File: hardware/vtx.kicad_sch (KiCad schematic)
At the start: 58 parts, among them J1 U.FL, Q27 BC857BM, Q28 AP1606, U19 RTC6705, U20 SE5004L, U21 LP5912-3.3, U22 LP5907-2.85, X4 8MHz 10pF

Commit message: wip: schematic integration in progress (saved after container restart)
Co-Authored-By: Claude Opus 5.5 <noreply@anthropic.com>
Claude-Session: https://claude.ai/code/session_01RFaS5jnC9tnPam9GBgmGnG
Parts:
- C108, C118: LCSC (none) -> C237279
- Q28: symbol OpenDrone:AP1606 -> lib:AP1606
- R84: value 10k -> 1k; LCSC C106225 -> (none); MPN RC0201FR-0710KL -> RC0201FR-071KL
- U21: symbol OpenDrone:LP5912-3.3DRVR -> lib:LP5912-3.3DRVR
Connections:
- net PA_RC1: now reaches C124.1, R71.2, R72.1
- net Q27_B: now reaches C125.1, Q27.1 (B), R72.2
- net U19_SPILE: now reaches R80.2, U19.6 (SPILE/CS1)
- net VT_MOD: now reaches R60.2, R61.2, R62.1, U19.10 (VT_Mod)
- net VT_MOD_N1: now reaches C104.2, C105.1, R58.2, R59.1
- net U19_XTAL2: now reaches C95.1, U19.25 (XTAL2), X4.3
- net Q27_E: now reaches Q27.2 (E), R73.2
- net VT_MOD_N2: now reaches C105.2, R60.1
- net U19_REG1D8: now reaches C96.1, U19.23 (REG1D8_1)
- net RTC_LF: now reaches C107.1, R64.2
- net U19_XTAL1: now reaches C94.1, U19.24 (XTAL1), X4.1
- net U19_SPICLK: now reaches R81.2, U19.7 (SPICLK/CS2)
- net RTC_CP: now reaches R63.1, U19.27 (CP)
- net RTC_VT: now reaches C106.1, R63.2, R64.1, U19.29 (VT)
- net U19_SPIDATA: now reaches R82.2, U19.5 (SPIDATA/CS0)
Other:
- moved on the sheet: R63, R80, R81, R82

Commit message: schematic: integrated (ERC 0 errors / 2 justified warnings; check_netlist 7/7; conventions 0 FAIL; visual 0 hits; 268/268 refs match bom_plan; FC+RX pin maps match PINMAP)
Co-Authored-By: Claude Opus 5.5 <noreply@anthropic.com>
Claude-Session: https://claude.ai/code/session_01RFaS5jnC9tnPam9GBgmGnG
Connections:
- net PA_BIAS_PWM renamed VTX_AMP_PWM
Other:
- note added: "PAOUT1 FEED"
- note added: "PNP PA DRIVE"
- note added: "RTC6705 VTX: 8 MHz CRYSTAL, SPI, VIDEO, PLL, PA DRIVE, PAOUT1 FEED"
- note added: "SE5004L PA + SUPPLY, DETECTOR, BPF + U.FL"
- note added: "SHEET NOTES"
- note removed: "PAOUT1 FEED + DC BLOCK"
- note removed: "PNP PA DRIVE STAGE"
- note removed: "RTC6705 + 8 MHz CRYSTAL"
- note removed: "SE5004L PA + SUPPLY"
- moved on the sheet: C122, C123, C124, C125, Q27, R71, R72, R73, U22

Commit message: hardware: floorplan v3 review pass (RX RF corner blocker fixed; majors listed in FLOORPLAN.md Open)
Co-Authored-By: Claude Opus 5.5 <noreply@anthropic.com>
Claude-Session: https://claude.ai/code/session_01RFaS5jnC9tnPam9GBgmGnG
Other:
- moved on the sheet: C100, C101, C102, C103, C104, C105, C106, C107, C109, C110, C111, C112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

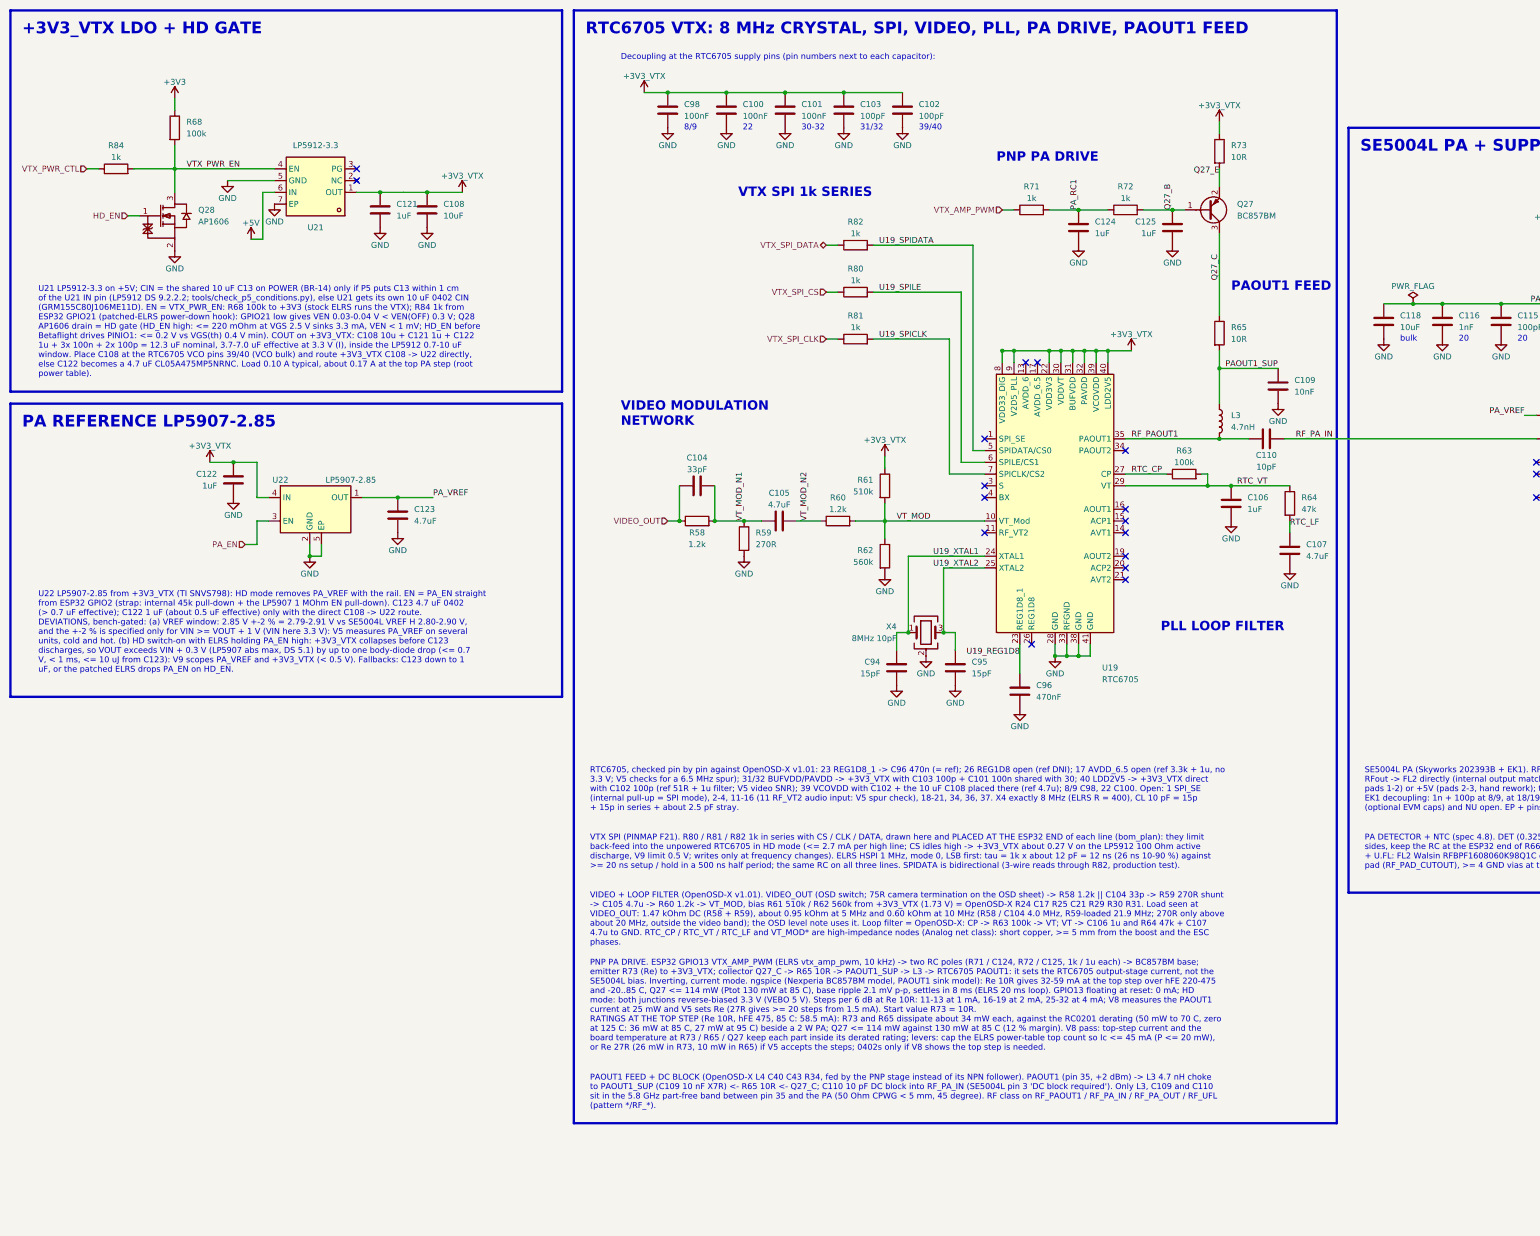
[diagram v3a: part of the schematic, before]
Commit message: wip: routing prep (zones and via fields) and schematic review round 4
Co-Authored-By: Claude Opus 5.5 <noreply@anthropic.com>
Claude-Session: https://claude.ai/code/session_01RFaS5jnC9tnPam9GBgmGnG
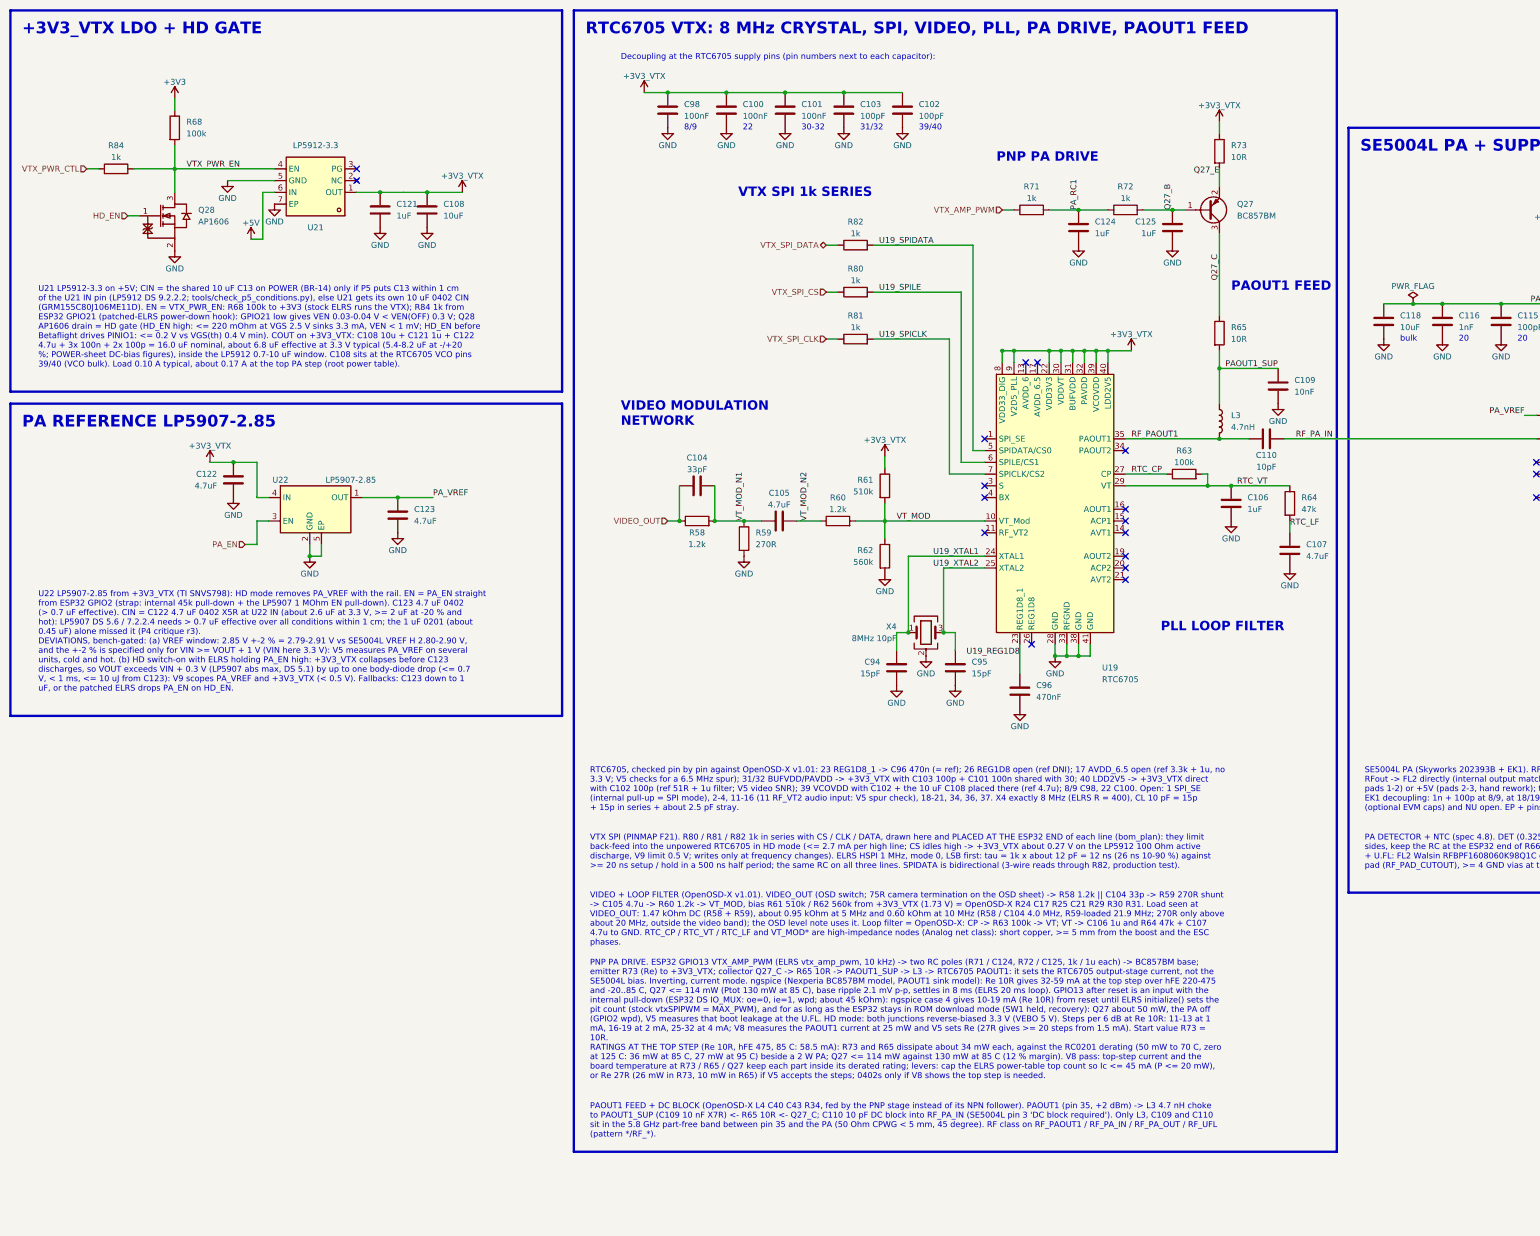
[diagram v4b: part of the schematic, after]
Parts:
- C122: value 1uF -> 4.7uF; footprint lib:C_0201_0603Metric_W -> lib:C_0402_1005Metric_W; LCSC C76935 -> C23733; MPN GRM033R61A105ME44D -> CL05A475MP5NRNC; Manufacturer Murata -> Samsung Electro-Mechanics
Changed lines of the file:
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@@
 	(rectangle
 		(start 137.16 27.94)
-		(end 302.26 268.74)
+		(end 302.26 274.92)
 		(stroke
 			(width 0.508)
@@
 	(rectangle
 		(start 15.24 113.03)
-		(end 134.62 176.48)
+		(end 134.62 180.6)
 		(stroke
 			(width 0.508)
@@
 		)
 	)
-	(text_box "U22 LP5907-2.85 from +3V3_VTX (TI SNVS798): HD mode removes PA_VREF with the rail. EN = PA_EN straight from ESP32 GPIO2 (strap: internal 45k pull-down + the LP5907 1 MOhm EN pull-down). C123 4.7 uF 0402 (> 0.7 uF effective); C122 1 uF (about 0.5 uF effective) only with the direct C108 -> U22 route.\nDEVIATIONS, bench-gated: (a) VREF window: 2.85 V +-2 % = 2.79-2.91 V vs SE5004L VREF H 2.80-2.90 V, and the +-2 % is specified only for VIN >= VOUT + 1 V (VIN here 3.3 V): V5 measures PA_VREF on several units, cold and hot. (b) HD switch-on with ELRS holding PA_EN high: +3V3_VTX collapses before C123 discharges, so VOUT exceeds VIN + 0.3 V (LP5907 abs max, DS 5.1) by up to one body-diode drop (<= 0.7 V, < 1 ms, <= 10 uJ from C123): V9 scopes PA_VREF and +3V3_VTX (< 0.5 V). Fallbacks: C123 down to 1 uF, or the patched ELRS drops PA_EN on HD_EN."
+	(text_box "U22 LP5907-2.85 from +3V3_VTX (TI SNVS798): HD mode removes PA_VREF with the rail. EN = PA_EN straight from ESP32 GPIO2 (strap: internal 45k pull-down + the LP5907 1 MOhm EN pull-down). C123 4.7 uF 0402 (> 0.7 uF effective). CIN = C122 4.7 uF 0402 X5R at U22 IN (about 2.6 uF at 3.3 V, >= 2 uF at -20 % and hot): LP5907 DS 5.6 / 7.2.2.4 needs > 0.7 uF effective over all conditions within 1 cm; the 1 uF 0201 (about 0.45 uF) alone missed it (P4 critique r3).\nDEVIATIONS, bench-gated: (a) VREF window: 2.85 V +-2 % = 2.79-2.91 V vs SE5004L VREF H 2.80-2.90 V, and the +-2 % is specified only for VIN >= VOUT + 1 V (VIN here 3.3 V): V5 measures PA_VREF on several units, cold and hot. (b) HD switch-on with ELRS holding PA_EN high: +3V3_VTX collapses before C123 discharges, so VOUT exceeds VIN + 0.3 V (LP5907 abs max, DS 5.1) by up to one body-diode drop (<= 0.7 V, < 1 ms, <= 10 uJ from C123): V9 scopes PA_VREF and +3V3_VTX (< 0.5 V). Fallbacks: C123 down to 1 uF, or the patched ELRS drops PA_EN on HD_EN."
 		(exclude_from_sim no)
 		(at 20.32 152.4 0)
-		(size 111.76 21.54)
+		(size 111.76 25.66)
 		(margins 0.9525 0.9525 0.9525 0.9525)
 		(stroke
@@
 		)
 	)
-	(text_box "U21 LP5912-3.3 on +5V; CIN = the shared 10 uF C13 on POWER (BR-14) only if P5 puts C13 within 1 cm of the U21 IN pin (LP5912 DS 9.2.2.2; tools/check_p5_conditions.py), else U21 gets its own 10 uF 0402 CIN (GRM155C80J106ME11D). EN = VTX_PWR_EN: R68 100k to +3V3 (stock ELRS runs the VTX); R84 1k from ESP32 GPIO21 (patched-ELRS power-down hook): GPIO21 low gives VEN 0.03-0.04 V < VEN(OFF) 0.3 V; Q28 AP1606 drain = HD gate (HD_EN high: <= 220 mOhm at VGS 2.5 V sinks 3.3 mA, VEN < 1 mV; HD_EN before Betaflight drives PINIO1: <= 0.2 V vs VGS(th) 0.4 V min). COUT on +3V3_VTX: C108 10u + C121 1u + C122 1u + 3x 100n + 2x 100p = 12.3 uF nominal, 3.7-7.0 uF effective at 3.3 V (I), inside the LP5912 0.7-10 uF window. Place C108 at the RTC6705 VCO pins 39/40 (VCO bulk) and route +3V3_VTX C108 -> U22 directly, else C122 becomes a 4.7 uF CL05A475MP5NRNC. Load 0.10 A typical, about 0.17 A at the top PA step (root power table)."
+	(text_box "U21 LP5912-3.3 on +5V; CIN = the shared 10 uF C13 on POWER (BR-14) only if P5 puts C13 within 1 cm of the U21 IN pin (LP5912 DS 9.2.2.2; tools/check_p5_conditions.py), else U21 gets its own 10 uF 0402 CIN (GRM155C80J106ME11D). EN = VTX_PWR_EN: R68 100k to +3V3 (stock ELRS runs the VTX); R84 1k from ESP32 GPIO21 (patched-ELRS power-down hook): GPIO21 low gives VEN 0.03-0.04 V < VEN(OFF) 0.3 V; Q28 AP1606 drain = HD gate (HD_EN high: <= 220 mOhm at VGS 2.5 V sinks 3.3 mA, VEN < 1 mV; HD_EN before Betaflight drives PINIO1: <= 0.2 V vs VGS(th) 0.4 V min). COUT on +3V3_VTX: C108 10u + C121 1u + C122 4.7u + 3x 100n + 2x 100p = 16.0 uF nominal, about 6.8 uF effective at 3.3 V typical (5.4-8.2 uF at -/+20 %; POWER-sheet DC-bias figures), inside the LP5912 0.7-10 uF window. C108 sits at the RTC6705 VCO pins 39/40 (VCO bulk). Load 0.10 A typical, about 0.17 A at the top PA step (root power table)."
 		(exclude_from_sim no)
 		(at 20.32 86.36 0)
@@
 		)
 	)
-	(text_box "PNP PA DRIVE. ESP32 GPIO13 VTX_AMP_PWM (ELRS vtx_amp_pwm, 10 kHz) -> two RC poles (R71 / C124, R72 / C125, 1k / 1u each) -> BC857BM base; emitter R73 (Re) to +3V3_VTX; collector Q27_C -> R65 10R -> PAOUT1_SUP -> L3 -> RTC6705 PAOUT1: it sets the RTC6705 output-stage current, not the SE5004L bias. Inverting, current mode. ngspice (Nexperia BC857BM model, PAOUT1 sink model): Re 10R gives 32-59 mA at the top step over hFE 220-475 and -20..85 C, Q27 <= 114 mW (Ptot 130 mW at 85 C), base ripple 2.1 mV p-p, settles in 8 ms (ELRS 20 ms loop). GPIO13 floating at reset: 0 mA; HD mode: both junctions reverse-biased 3.3 V (VEBO 5 V). Steps per 6 dB at Re 10R: 11-13 at 1 mA, 16-19 at 2 mA, 25-32 at 4 mA; V8 measures the PAOUT1 current at 25 mW and V5 sets Re (27R gives >= 20 steps from 1.5 mA). Start value R73 = 10R.\nRATINGS AT THE TOP STEP (Re 10R, hFE 475, 85 C: 58.5 mA): R73 and R65 dissipate about 34 mW each, against the RC0201 derating (50 mW to 70 C, zero at 125 C: 36 mW at 85 C, 27 mW at 95 C) beside a 2 W PA; Q27 <= 114 mW against 130 mW at 85 C (12 % margin). V8 pass: top-step current and the board temperature at R73 / R65 / Q27 keep each part inside its derated rating; levers: cap the ELRS power-table top count so Ic <= 45 mA (P <= 20 mW), or Re 27R (26 mW in R73, 10 mW in R65) if V5 accepts the steps; 0402s only if V8 shows the top step is needed."
+	(text_box "PNP PA DRIVE. ESP32 GPIO13 VTX_AMP_PWM (ELRS vtx_amp_pwm, 10 kHz) -> two RC poles (R71 / C124, R72 / C125, 1k / 1u each) -> BC857BM base; emitter R73 (Re) to +3V3_VTX; collector Q27_C -> R65 10R -> PAOUT1_SUP -> L3 -> RTC6705 PAOUT1: it sets the RTC6705 output-stage current, not the SE5004L bias. Inverting, current mode. ngspice (Nexperia BC857BM model, PAOUT1 sink model): Re 10R gives 32-59 mA at the top step over hFE 220-475 and -20..85 C, Q27 <= 114 mW (Ptot 130 mW at 85 C), base ripple 2.1 mV p-p, settles in 8 ms (ELRS 20 ms loop). GPIO13 after reset is an input with the internal pull-down (ESP32 DS IO_MUX: oe=0, ie=1, wpd; about 45 kOhm): ngspice case 4 gives 10-19 mA (Re 10R) from reset until ELRS initialize() sets the pit count (stock vtxSPIPWM = MAX_PWM), and for as long as the ESP32 stays in ROM download mode (SW1 held, recovery): Q27 about 50 mW, the PA off (GPIO2 wpd), V5 measures that boot leakage at the U.FL. HD mode: both junctions reverse-biased 3.3 V (VEBO 5 V). Steps per 6 dB at Re 10R: 11-13 at 1 mA, 16-19 at 2 mA, 25-32 at 4 mA; V8 measures the PAOUT1 current at 25 mW and V5 sets Re (27R gives >= 20 steps from 1.5 mA). Start value R73 = 10R.\nRATINGS AT THE TOP STEP (Re 10R, hFE 475, 85 C: 58.5 mA): R73 and R65 dissipate about 34 mW each, against the RC0201 derating (50 mW to 70 C, zero at 125 C: 36 mW at 85 C, 27 mW at 95 C) beside a 2 W PA; Q27 <= 114 mW against 130 mW at 85 C (12 % margin). V8 pass: top-step current and the board temperature at R73 / R65 / Q27 keep each part inside its derated rating; levers: cap the ELRS power-table top count so Ic <= 45 mA (P <= 20 mW), or Re 27R (26 mW in R73, 10 mW in R65) if V5 accepts the steps; 0402s only if V8 shows the top step is needed."
 		(exclude_from_sim no)
 		(at 139.7 232.15 0)
-		(size 160.02 23.6)
+		(size 160.02 29.78)
 		(margins 0.9525 0.9525 0.9525 0.9525)
 		(stroke
@@
 	(text_box "PAOUT1 FEED + DC BLOCK (OpenOSD-X L4 C40 C43 R34, fed by the PNP stage instead of its NPN follower). PAOUT1 (pin 35, +2 dBm) -> L3 4.7 nH choke to PAOUT1_SUP (C109 10 nF X7R) <- R65 10R <- Q27_C; C110 10 pF DC block into RF_PA_IN (SE5004L pin 3 'DC block required'). Only L3, C109 and C110 sit in the 5.8 GHz part-free band between pin 35 and the PA (50 Ohm CPWG < 5 mm, 45 degree). RF class on RF_PAOUT1 / RF_PA_IN / RF_PA_OUT / RF_UFL (pattern */RF_*)."
 		(exclude_from_sim no)
-		(at 139.7 257.02 0)
+		(at 139.7 263.2 0)
 		(size 160.02 9.18)
 		(margins 0.9525 0.9525 0.9525 0.9525)
@@
 			)
 		)
-		(property "Value" "1uF"
+		(property "Value" "4.7uF"
 			(at 59.968 130.81 0)
 			(show_name no)
@@
 			)
 		)
-		(property "Footprint" "lib:C_0201_0603Metric_W"
+		(property "Footprint" "lib:C_0402_1005Metric_W"
 			(at 63.5 129.54 0)
 			(hide yes)
@@
 			)
 		)
-		(property "LCSC" "C76935"
+		(property "LCSC" "C23733"
 			(at 63.5 129.54 0)
 			(hide yes)
@@
 			)
 		)
-		(property "MPN" "GRM033R61A105ME44D"
+		(property "MPN" "CL05A475MP5NRNC"
 			(at 63.5 129.54 0)
 			(hide yes)
@@
 			)
 		)
-		(property "Manufacturer" "Murata"
+		(property "Manufacturer" "Samsung Electro-Mechanics"
 			(at 63.5 129.54 0)
 			(hide yes)

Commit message: schematic: review complete (4 rounds; U20 pin 1 to GND, footprint filters fixed, TPS22810DRVR, R54 270R); ERC 0 errors, check_netlist 7/7; D85-D87
Co-Authored-By: Claude Opus 5.5 <noreply@anthropic.com>
Claude-Session: https://claude.ai/code/session_01RFaS5jnC9tnPam9GBgmGnG
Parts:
- R68: value 100k -> 47k; LCSC C106224 -> (none); MPN RC0201FR-07100KL -> RC0201FR-0747KL
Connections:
- net GND: now also U20.1 (NU)
- no-connect marks 19 -> 18
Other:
- moved on the sheet: C122, C123, U22

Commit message: WIP final schematic (D111/D113): GPIO map, D100 oscillator, final footprints, lineup power-net names; mid-run snapshot, not yet verified (ERC/netlist/DRU regen pending)
Co-Authored-By: Claude Opus 5.5 <noreply@anthropic.com>
Claude-Session: https://claude.ai/code/session_01RFaS5jnC9tnPam9GBgmGnG
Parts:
- C100, C101, C102, C103, C104, C109, C110, C111, C112, C113, C114, C115, C116, C117, C121, C124, C125, C94, C95, C96, C98: footprint lib:C_0201_0603Metric_W -> lib:C_0201_0603Metric_L
- C105, C106, C107, C108, C118, C122, C123: footprint lib:C_0402_1005Metric_W -> lib:C_0402_1005Metric_L
- J1: footprint lib:U.FL_Hirose_U.FL-R-SMT-1_Vertical -> lib:U.FL_Hirose_U.FL-R-SMT-1_Vertical_L
- L3: footprint lib:L_0201_0603Metric_W -> lib:L_0201_0603Metric_L
- R58, R59, R60, R61, R62, R63, R64, R65, R66, R68, R70, R71, R72, R73, R80, R81, R82, R84, TH1: footprint lib:R_0201_0603Metric_W -> lib:R_0201_0603Metric_L
- R67: footprint lib:R_0402_Selector_3Pad -> lib:R_0402_Selector_3Pad_L
- U19: footprint lib:QFN-40_6x6mm_P0.5mm_EP_RTC6705_Dense -> lib:QFN-40_6x6mm_P0.5mm_EP_RTC6705_L
- U20: footprint lib:QFN-20_4x4mm_P0.5mm_EP_SE5004L -> lib:QFN-20_4x4mm_P0.5mm_EP_SE5004L_L
- U21: footprint lib:WSON-6-1EP_2x2mm_P0.65mm_EP1x1.6mm_Dense -> lib:WSON-6-1EP_2x2mm_P0.65mm_EP1x1.6mm_L
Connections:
- net +3V3 renamed +3.3V
- net +3V3_VTX renamed +3.3V_VTX
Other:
- note added: "+3.3V_VTX LDO + HD GATE"
- note removed: "+3V3_VTX LDO + HD GATE"
